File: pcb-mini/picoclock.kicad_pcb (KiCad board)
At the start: 4 copper layers, 140 x 54 mm, 142 parts, among them J1 UART, J10 USB, J11 Alt Power, J12 LED_5V, J13 ESP32_IO0, J14 SJ2-35863B1-SMT-TR, J15 Conn_01x24, J2 USB_A, J3 UART, J4 xx, J5 Micro_SD_Card_Det1, J6 USB_C_Receptacle, J7 DBG, J8 Conn_01x21_Pin, J9 AUDIO, Q1 BSS138, Q3 BSS138, SW1 SW_Push, SW2 SW_Push, SW3 SW_Push, SW4 SW_Push, SW5 SW_Push, SW6 SW_Push, SW7 SW_Push, U1 PCF8563T, U10 74LS157, U12 ENS160, U13 TCR2EE19, U2 RP2350_80QFN, U3 MCP9808_MSOP, U4 PCM5100, U5 PAM8302A, U6 W25Q128JVS, U7 MCP45X1-104E, U8 NCP1117-3.3_SOT223, U9 ESP32-WROOM-E, Y1 Crystal, Y2 ABM8-272-T3

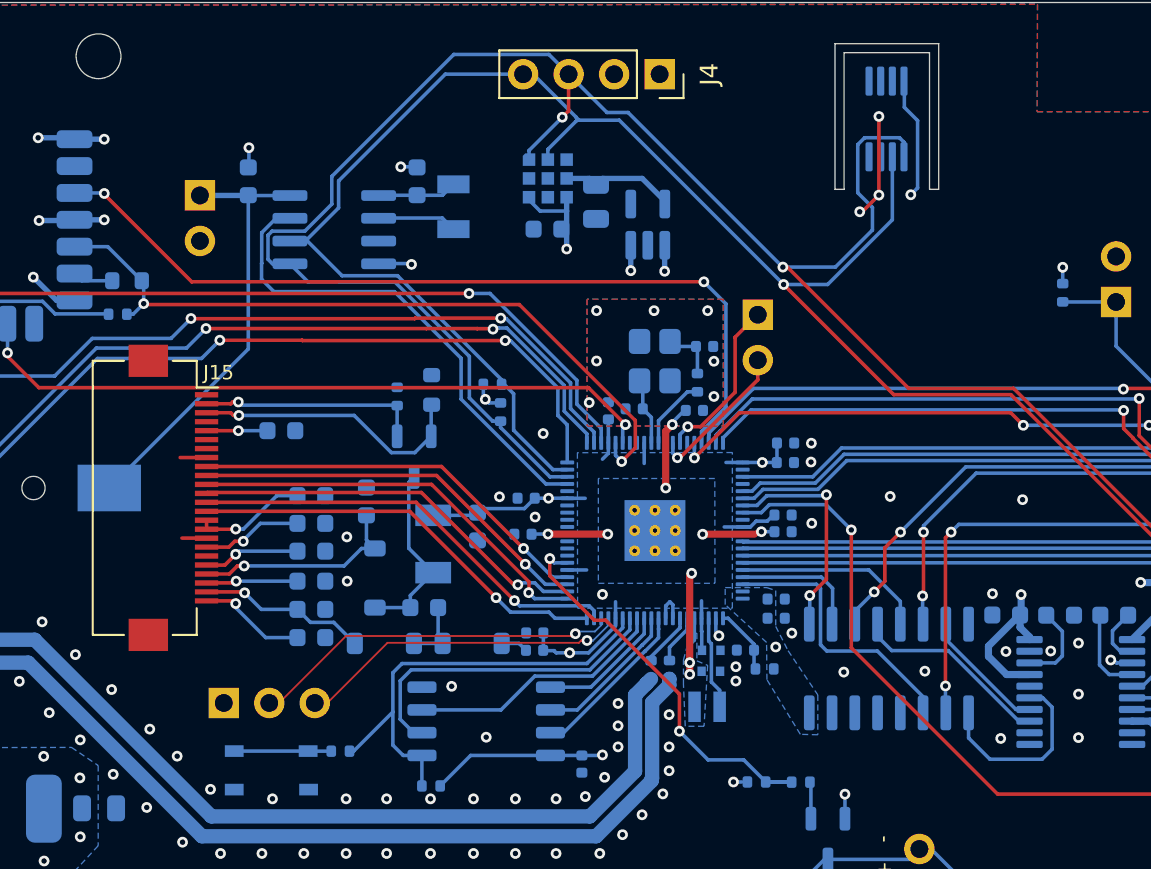
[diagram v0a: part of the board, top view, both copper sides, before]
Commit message: [pcb] mini: RTC: add diods, wire INT. fix 74LS chip footprint
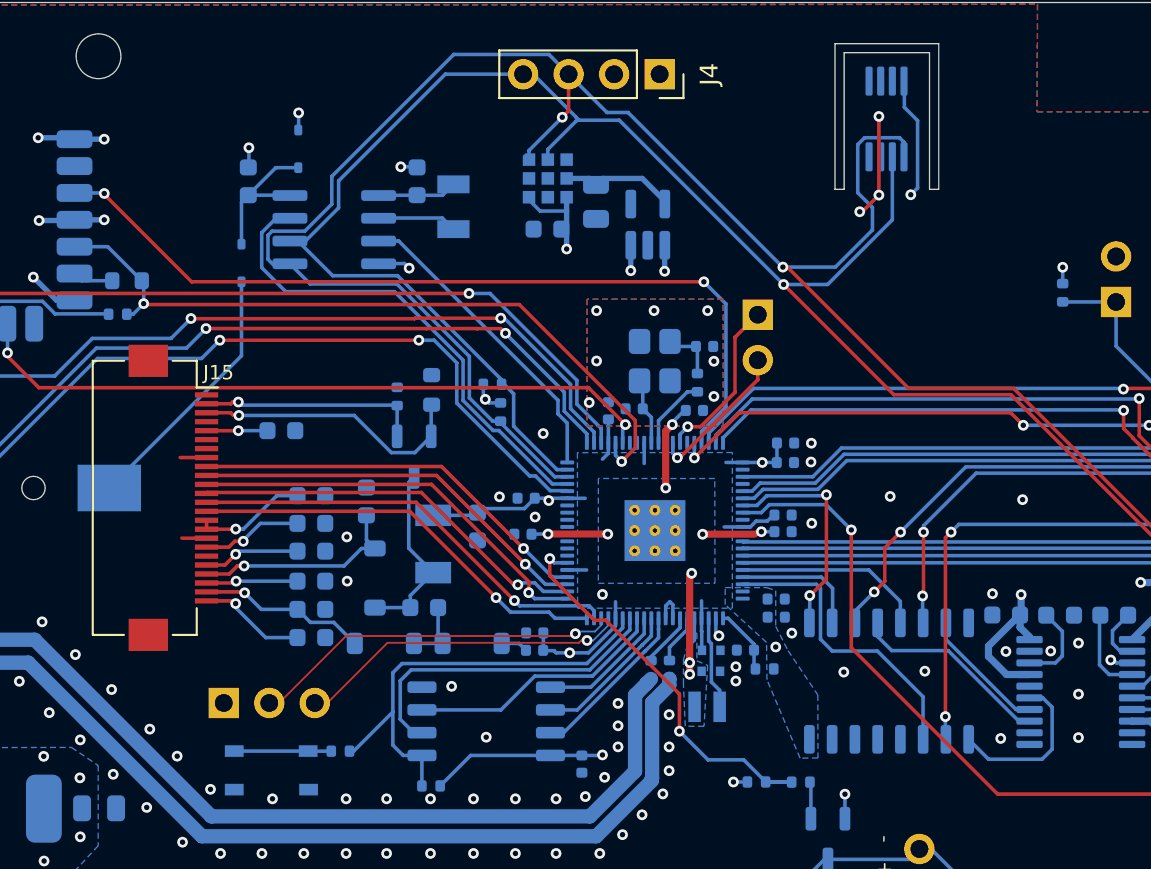
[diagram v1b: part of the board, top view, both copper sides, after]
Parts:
- removed J11: Alt Power, Connector_PinHeader_2.54mm:PinHeader_1x02_P2.54mm_Vertical
- added D10: SS12, Diode_SMD:D_SOD-323, B.Cu at (129.9, 88.2)
- added D11: SS12, Diode_SMD:D_SOD-323, B.Cu at (126.8, 94.5)
- U10: footprint Package_SO:SOIC-16_3.9x9.9mm_P1.27mm -> Package_SO:SOP-16_4.55x10.3mm_P1.27mm
- moved U10 0.71 mm to (162.9, 117.9)
- moved C41 0.06 mm to (156.6, 114.3)
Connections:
- C2 pad 1: 3V BATT -> Net-(D10-K)
- U1 pad 8: 3V BATT -> Net-(D10-K)
- U2 pad 16: unconnected-(U2-GPIO16-Pad16) -> GPIO20/btn
- U2 pad 20: GPIO20/btn -> 1~{PRE}
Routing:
- net 1~{PRE}: track 0.00 -> 17.4 mm
- net 3V BATT: track 24.6 -> 14.6 mm
- net Net-(D10-K): track 0.00 -> 8.67 mm
- net BT_I2S_LRCK: track 53.4 -> 55.3 mm
- net /LRCK: track 10.6 -> 9.26 mm
- net PICO_LRCK: track 15.4 -> 16.7 mm
- net +3V3: track 110.2 -> 111.3 mm, vias 38 -> 39

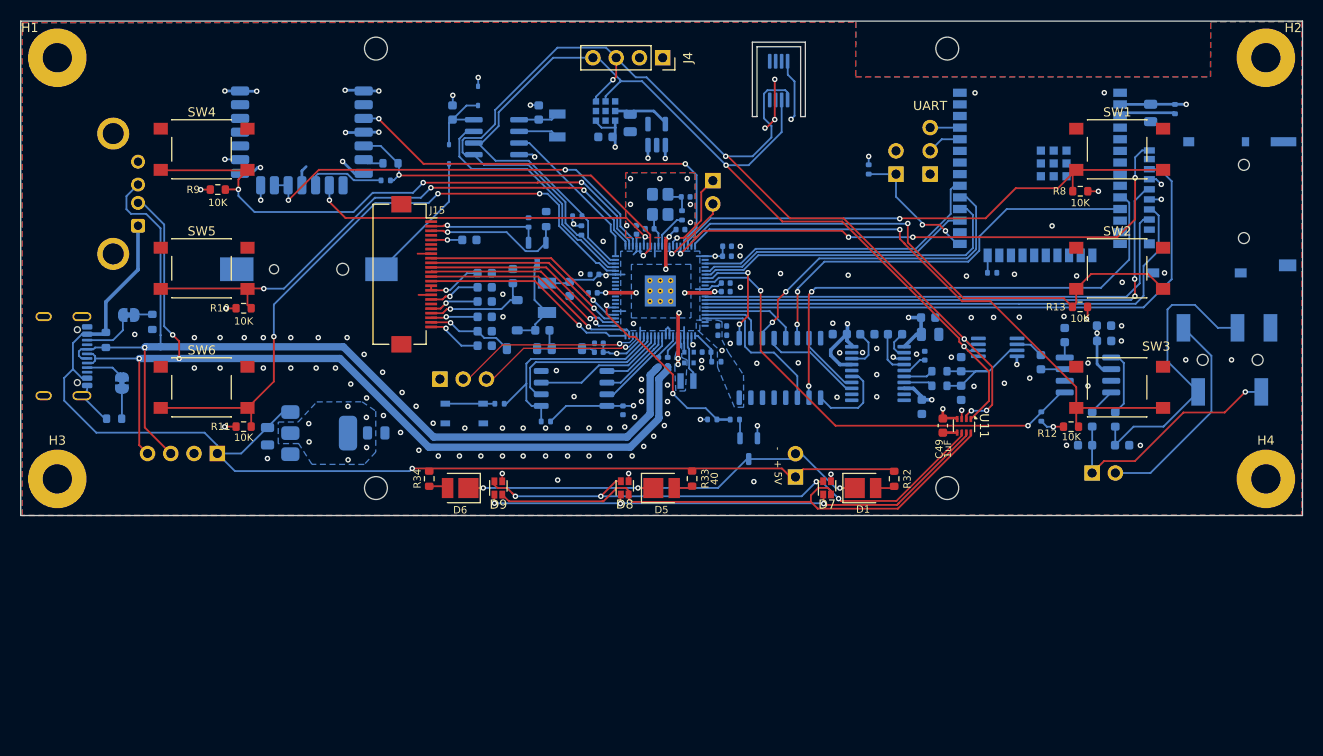
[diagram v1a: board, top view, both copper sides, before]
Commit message: [pcb] mini: move boot btn, add silkscreen, add con for ESP32 UART
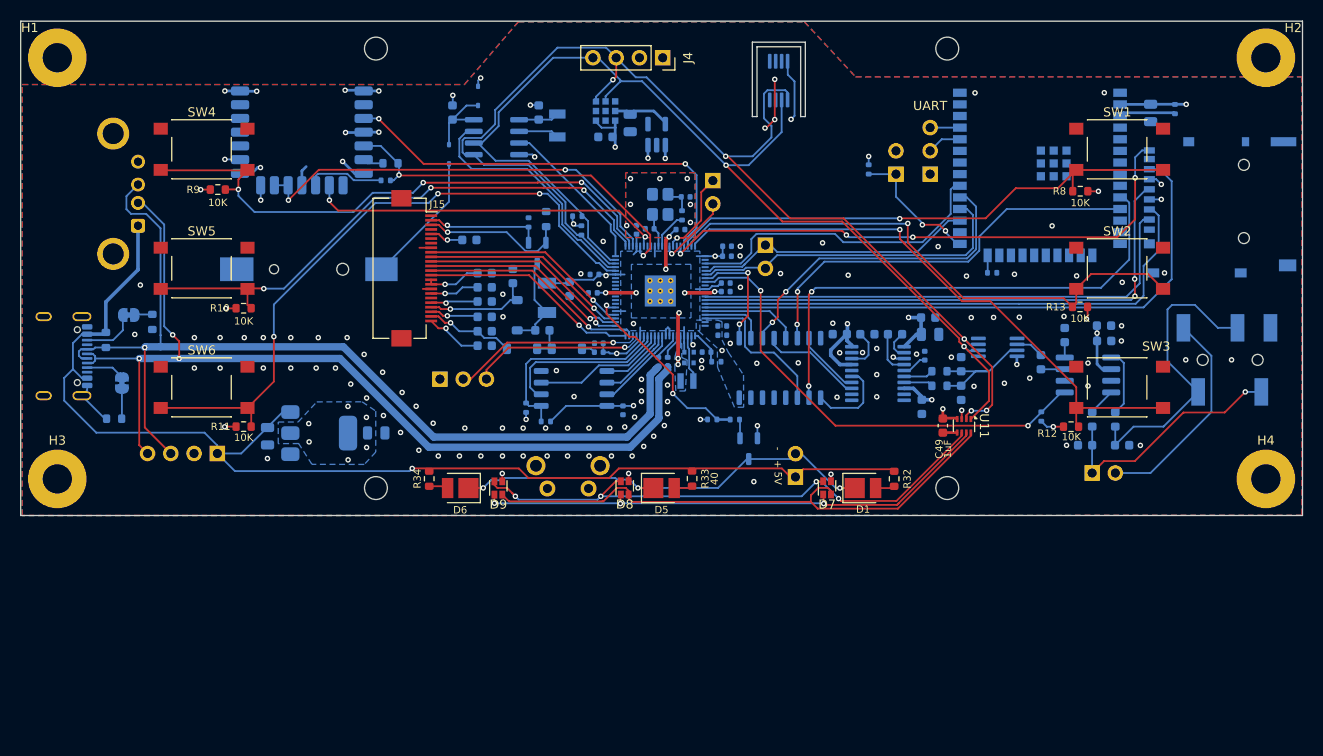
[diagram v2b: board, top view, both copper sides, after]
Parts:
- added J11: ESP32_UART1, Connector_PinHeader_2.54mm:PinHeader_1x02_P2.54mm_Vertical, B.Cu at (161.3, 104.5)
- SW7: footprint Button_Switch_SMD:SW_Push_1P1T_NO_Vertical_Wuerth_434133025816 -> Button_Switch_THT:SW_Tactile_SPST_Angled_PTS645Vx31-2LFS
- moved SW7 12.2 mm to (137.5, 131.1)
- moved R15 2.93 mm to (135.2, 122.2), turned to -90 degrees
- moved J15 0.65 mm to (123.0, 107.0)
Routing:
- net /uC/~{USB_BOOT}: track 5.42 -> 11.2 mm, vias 0 -> 1
- net /uC/FLASH_SS: track 25.3 -> 22.2 mm
- net GPIO34_ESP32_COM: track 32.9 -> 34.6 mm
- net LED_5V-: track 47.6 -> 48.5 mm
- net LED_5V+: track 131.0 -> 131.8 mm
- net GND: track 45.4 -> 44.7 mm, vias 130 -> 132
- net ESP32_UART1_RX: track 30.1 -> 30.7 mm
- net GPIO0_TX: track 19.1 -> 19.7 mm
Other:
- board text added: "BCK"
- board text added: "DIN"
- board text added: "LRCK"

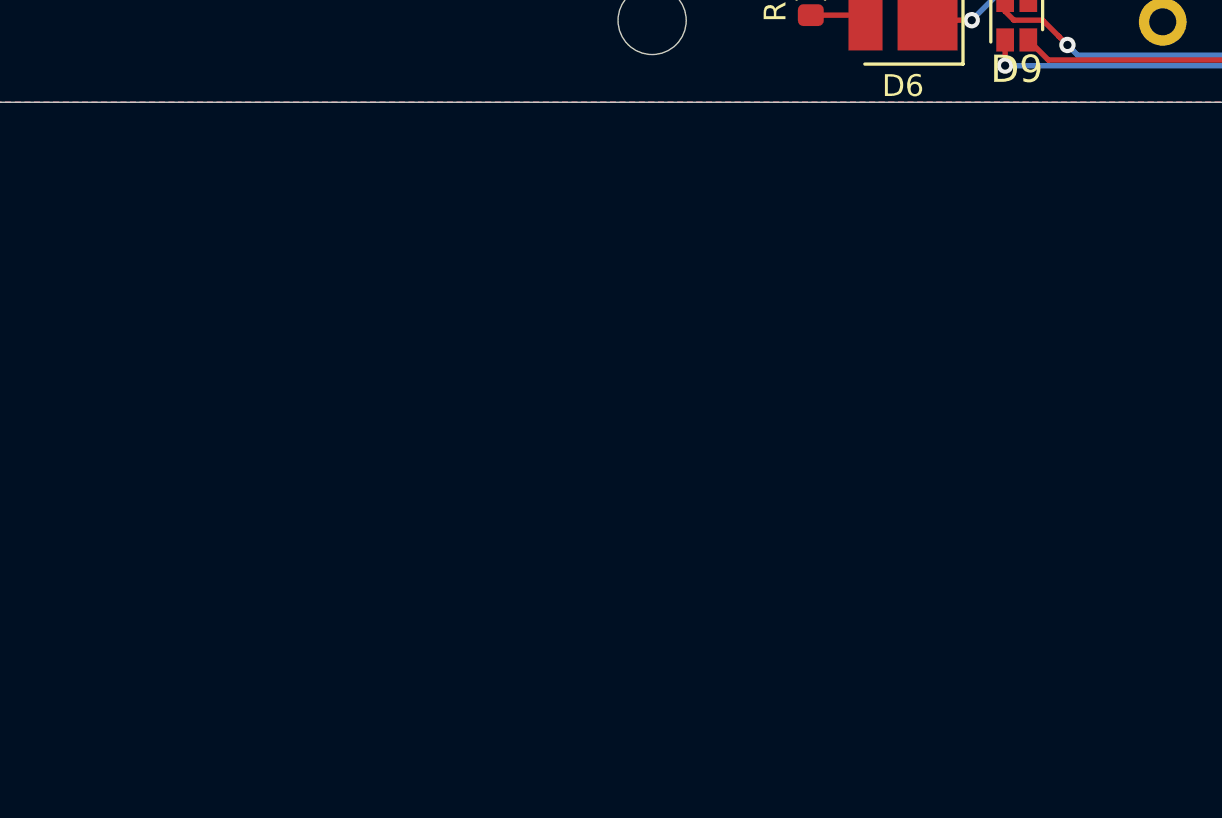
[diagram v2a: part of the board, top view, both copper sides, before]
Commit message: [pcb] mini: add senseair schema+footprint
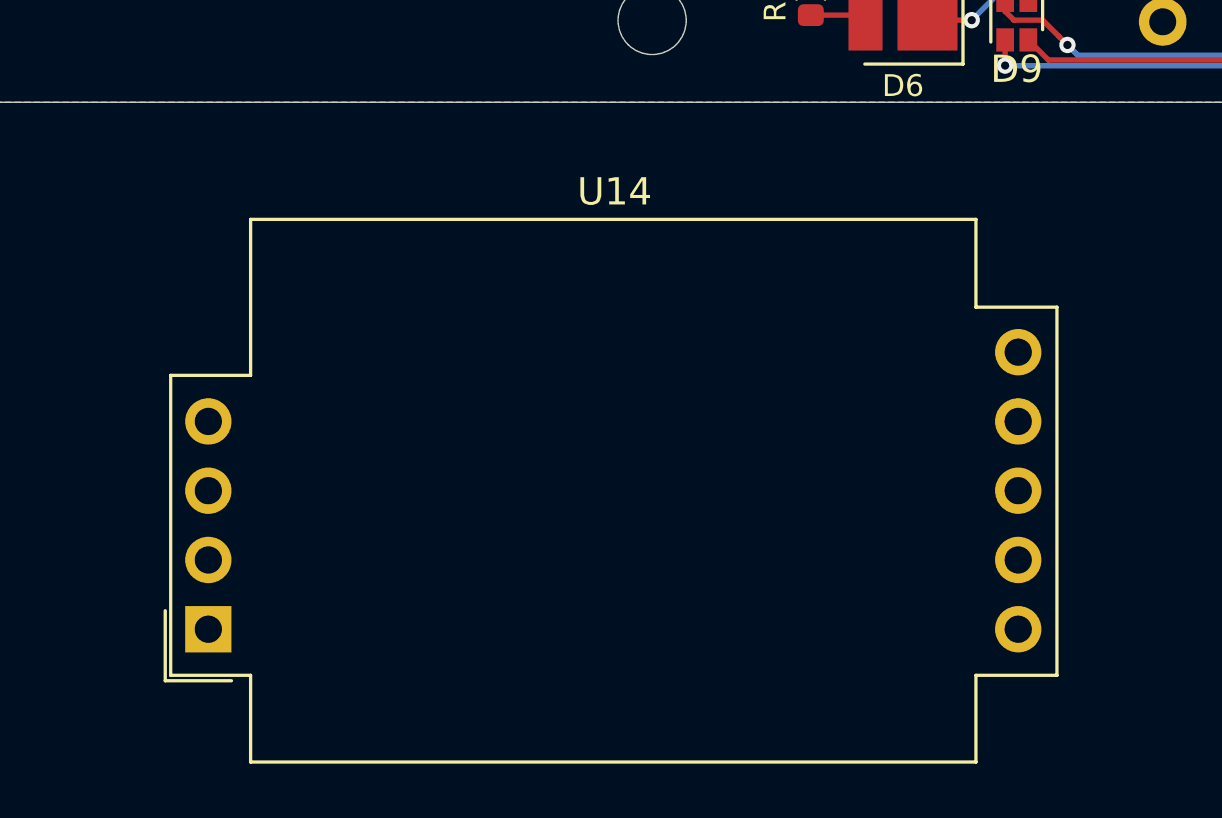
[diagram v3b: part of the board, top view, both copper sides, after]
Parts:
- added U14: 004-0-0075, senseair:Senseair_S8_Down, F.Cu at (102.5, 153.3)

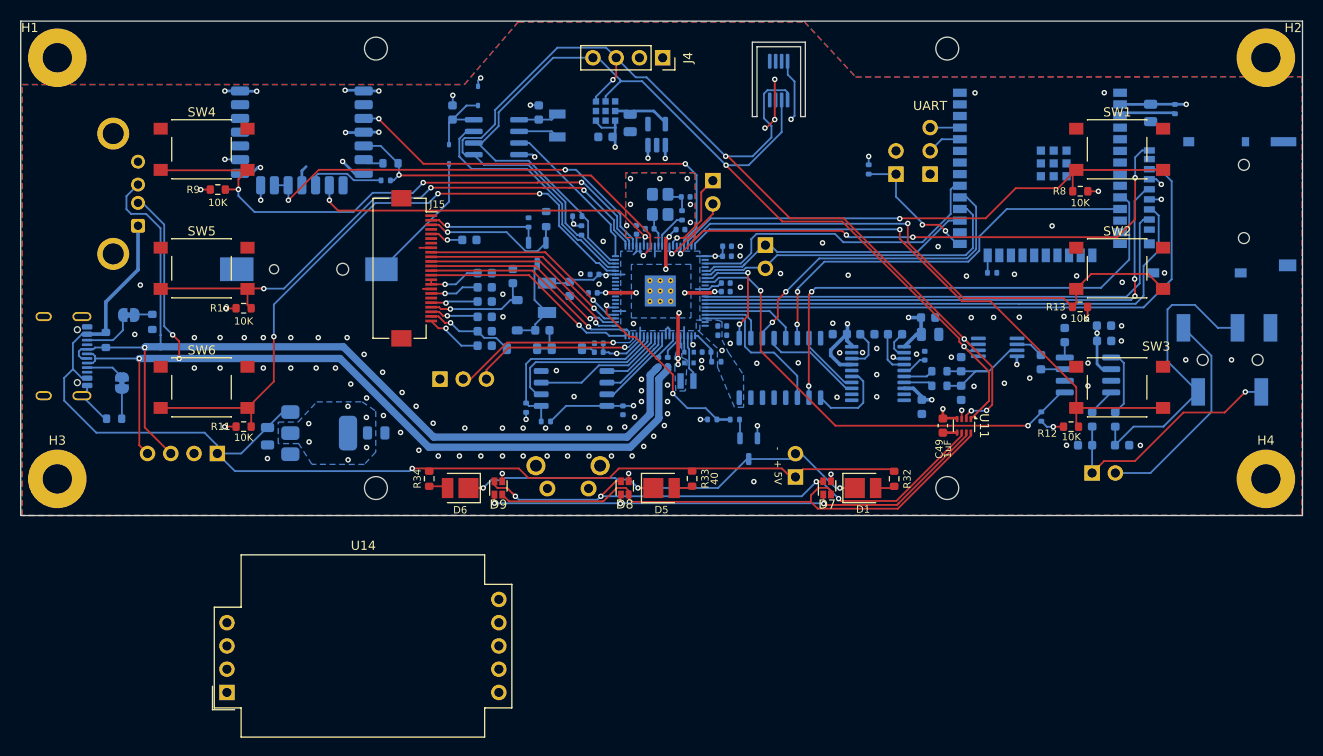
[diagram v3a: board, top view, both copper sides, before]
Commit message: [pcb] mini: add SHT40 + senseair S88 connectors
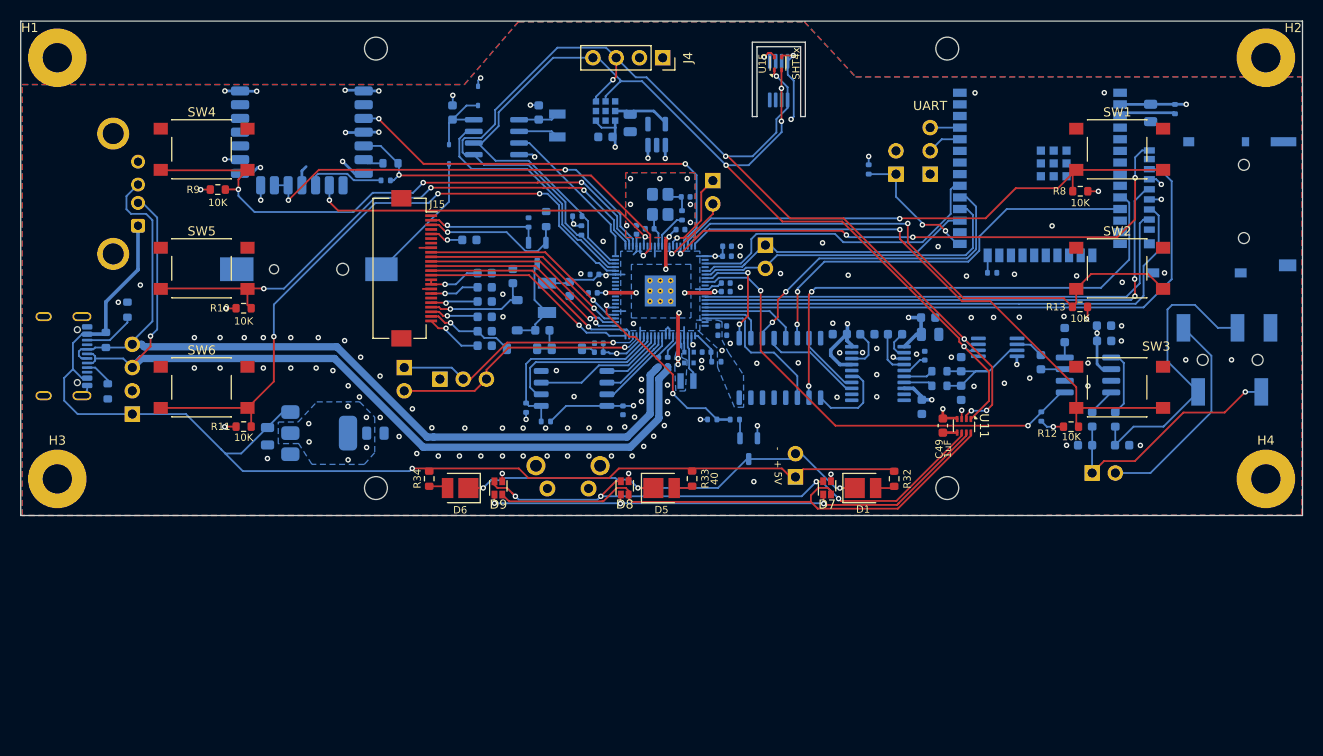
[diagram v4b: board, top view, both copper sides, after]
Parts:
- removed JP1, JP2: SJB, Jumper:SolderJumper-2_P1.3mm_Bridged_RoundedPad1.0x1.5mm
- removed U14: 004-0-0075, senseair:Senseair_S8_Down
- added J16: UART_S88, Connector_PinHeader_2.54mm:PinHeader_1x02_P2.54mm_Vertical, B.Cu at (121.9, 117.8)
- added U15: SHT4x, Sensor_Humidity:Sensirion_DFN-4_1.5x1.5mm_P0.8mm_SHT4x_NoCentralPad, F.Cu at (162.7, 84.6)
- moved J10 10.2 mm to (92.2, 122.9), turned to 0 degrees
- moved R6 3.06 mm to (89.5, 120.4), turned to -90 degrees
- moved R5 3.03 mm to (91.7, 111.5), turned to 90 degrees
- moved C47 0.09 mm to (118.7, 125.0)
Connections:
- J10 pad 3: USB D+ -> USB D-
- J10 pad 4: USB D- -> USB D+
- R5 pad 1: Net-(JP2-A) -> Net-(J6-CC2)
- R6 pad 1: Net-(JP1-A) -> Net-(J6-CC1)
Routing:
- net USB D+: track 108.3 -> 96.0 mm, vias 1 -> 0
- net GPIO0_TX: track 19.7 -> 29.2 mm
- net USB D-: track 105.3 -> 96.1 mm, vias 3 -> 1
- net GND: track 44.7 -> 36.3 mm, vias 132 -> 129
- net GPIO1_RX: track 20.7 -> 27.7 mm
- net SCL: track 119.2 -> 123.8 mm, vias 2 -> 4
- net Net-(JP1-A): track 3.26 -> 0.00 mm
- net Net-(JP2-A): track 2.45 -> 0.00 mm
- net +3V3: track 111.3 -> 113.5 mm, vias 39 -> 40
- net LED_5V+: track 131.8 -> 130.5 mm
- net Net-(J6-CC1): track 4.22 -> 3.22 mm
- net SDA: vias 5 -> 6

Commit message: [pcb] mini: move audio into dedicated sheet
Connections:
- net /BCK renamed /audio/BCK
- net /DIN renamed /audio/DIN
- net /LRCK renamed /audio/LRCK
